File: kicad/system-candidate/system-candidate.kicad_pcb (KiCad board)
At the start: 4 copper layers, 153 x 79.1 mm, 204 parts, among them J1 691137710002 2P 5.00mm, J2 Auxiliary 12V, J3 Differential audio, J301 T1_SECONDARY, J4 Control 2x4: 3V3 RESET FAULT 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, J401 START_BUTTON, J5 691137710002 2P 5.00mm, J6 GND braid solder bond - NO mo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, K501 G6K-2F DC12, Q501 MMBT3904, Q502 MMBT3904, U1 TPA3255DDV, U2 OPA1656ID, U3 OPA1656ID, U302 LM5164DDA, U303 TPS3700DDC, U401 LP2985-33, U402 TPS3808G33, U403 TPS3808G33, U404 TPS3808G33, U405 74LVC1G14, U406 74LVC2G74, U407 74LVC2G74, U408 74LVC1G32, U409 74LVC1G07, U410 74LVC1G08, U411 74LVC1G06, U412 TPS3700DDC, U413 TPS3700DDC, U414 TPS3808G33, U415 74LVC1G08, U416 TPS3808G33, U417 74LVC2G74, U418 74LVC1G32, U419 74LVC1G07, U501 TPS3700DDC, U502 TPS3700DDC, U503 TMUX6219, U504 TPS3700DDC

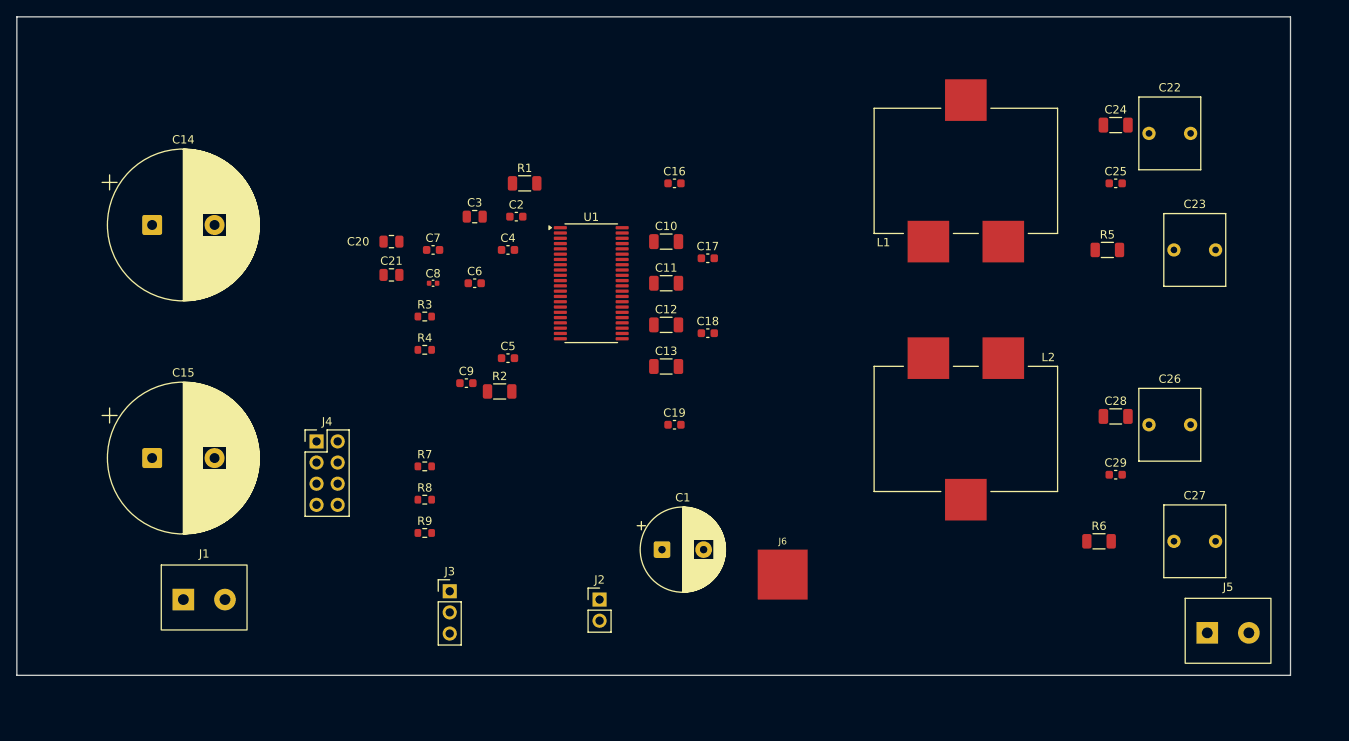
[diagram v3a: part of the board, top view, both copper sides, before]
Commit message: feat(pcb): apply measured OEM outline, M3 holes and U-profile keepout to system candidate
154x81 mm outline, 4 board-only M3 holes and F.Cu rule area OEM_U_PROFILE replace the inferred 153x79.1 study outline. DRC now shows 34 real placement conflicts (core parts inside the profile, J5 on H3): PCB-001 worklist.
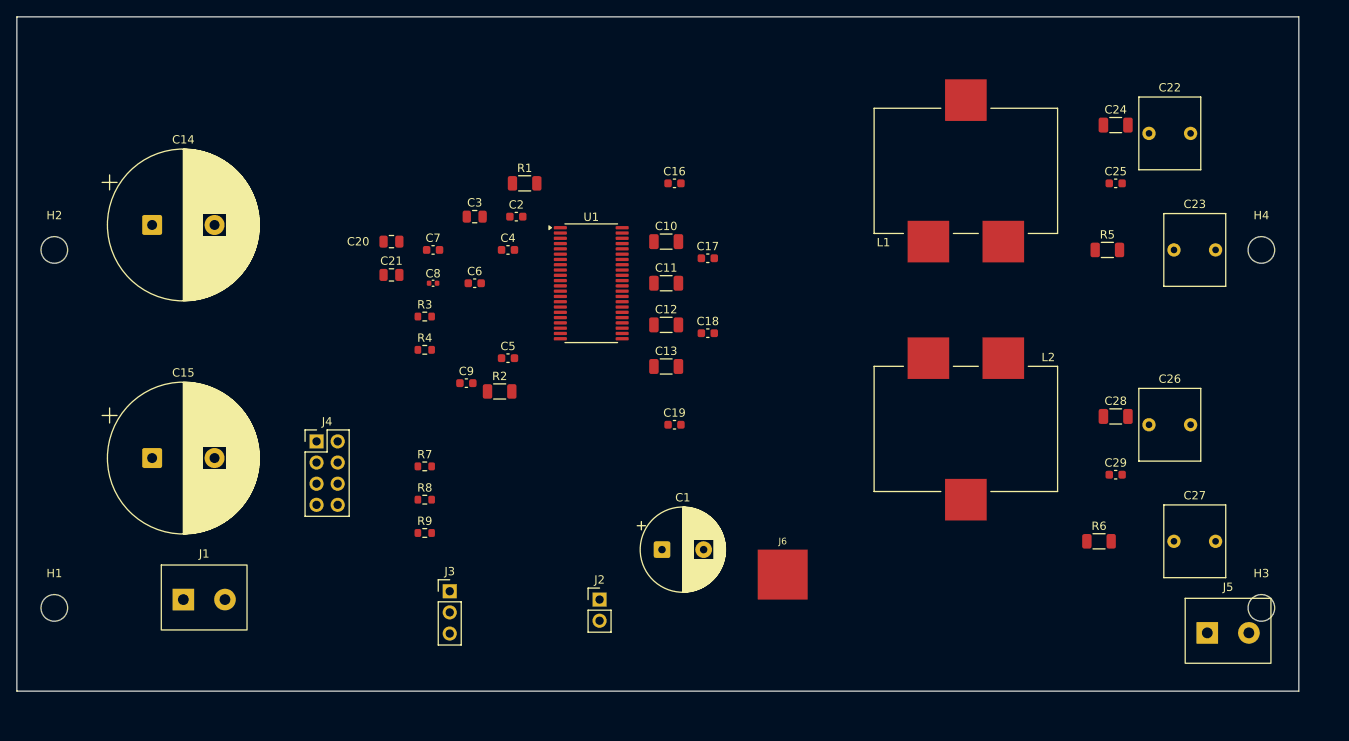
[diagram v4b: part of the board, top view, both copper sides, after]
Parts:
- added H1: OEM L-bracket M3, MountingHole:MountingHole_3.2mm_M3, F.Cu at (24.5, 91.0)
- added H2: OEM L-bracket M3, MountingHole:MountingHole_3.2mm_M3, F.Cu at (24.5, 48.0)
- added H3: OEM L-bracket M3, MountingHole:MountingHole_3.2mm_M3, F.Cu at (169.5, 91.0)
- added H4: OEM L-bracket M3, MountingHole:MountingHole_3.2mm_M3, F.Cu at (169.5, 48.0)
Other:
- board size 153 x 79.1 mm -> 154 x 81 mm
- board text added: "MEASURED OEM 154x81 (TAPE, ~1 mm) - NOT FABRICATION"
- board text added: "OEM U PROFILE 65x33 - BASE ON PCB - NO TOP PARTS"
- board text added: "TO-3P M3 (LEG FACE)"
- board text removed: "LEFT_LOWER / NO DRILL"
- board text removed: "LEFT_UPPER / NO DRILL"
- board text removed: "NO INFERRED MOUNT HOLES; J6 = SOLDERED GND BOND"
- board text removed: "OEM STUDY - 2 X CALIBRATION - NOT FABRICATION / MOUNT FIT UNVERIFIED"
- board text removed: "RIGHT FRAME STRIP: EDGE UNRESOLVED"
- board text removed: "RIGHT_LOWER / NO DRILL"
- board text removed: "RIGHT_UPPER / NO DRILL"
- board text removed: "THERMAL_LEFT / NO DRILL"
- board text removed: "THERMAL_RIGHT / NO DRILL"

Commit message: feat(pcb): study placement of all 204 parts in the measured OEM outline
Owner-confirmed orientation (x=20 relay end, x=174 transformer end). place_system_candidate.py packs power/THT on top and logic/analog SMD on the bottom; TPA3255 beside the U-profile leg. DRC: silkscreen only. README shows the latest 3D render.
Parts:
- C107, C108, C401, C402, C403, C404, C405, C406, C407, C408, C409, C410, C411, C412, C413, C414, C415, C416, C417, C418, C419, C420, C421, C422, C423, C503, C504, C505, C506, C507, C508, C509, C510, C511, C512, D501, D502, D503, D504, Q501, Q502, R101, R102, R103, R104, R105, R106, R107, R108, R202, R203, R204, R205, R206, R207, R401, R402, R403, R404, R405, R406, R407, R408, R420, R421, R422, R423, R424, R425, R426, R427, R428, R429, R430, R501, R502, R503, R504, R505, R506, R507, R508, R509, R510, R511, R512, R513, R514, R515, R516, R517, R518, U2, U3, U401, U402, U403, U404, U405, U406, U407, U408, U409, U410, U411, U412, U413, U414, U415, U416, U417, U418, U419, U501, U502, U503, U504: moved to B.Cu
- moved C410 527.6 mm to (48.4, 33.1), turned to 90 degrees
- moved U403 525.2 mm to (49.0, 37.9), turned to 90 degrees
- moved R511 518.5 mm to (85.6, 70.9)
- moved U408 517.4 mm to (56.6, 55.5)
- moved R423 509.6 mm to (70.4, 54.9), turned to 90 degrees
- moved U416 509.3 mm to (66.8, 50.9), turned to 90 degrees
- moved C421 508.2 mm to (72.1, 34.9), turned to 90 degrees
- moved R406 506.7 mm to (45.4, 34.1), turned to 90 degrees
- moved U502 506.2 mm to (89.9, 57.2)
- moved C510 503.3 mm to (94.1, 73.1)
- moved C420 502.2 mm to (52.9, 59.1)
- moved C508 501.5 mm to (89.9, 70.1)
- moved R422 500.4 mm to (57.1, 59.1)
- moved U503 497.0 mm to (90.0, 61.9)
- moved R407 496.4 mm to (77.6, 49.1), turned to 90 degrees
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
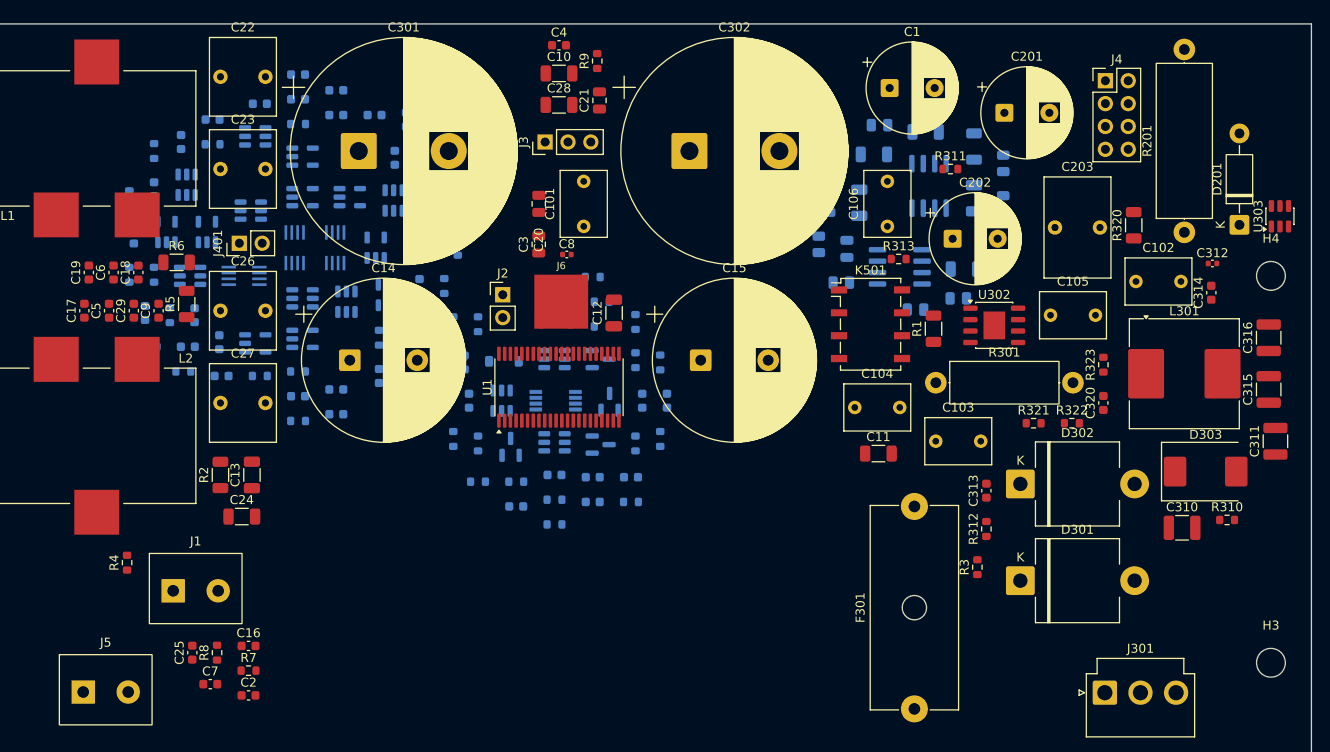
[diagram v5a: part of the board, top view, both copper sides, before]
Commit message: feat(pcb): autoroute system candidate and add datasheet envelope 3D models
make route-system: Freerouting 1.9.0 under Xvfb, 4 layers with In1 GND plane, 463/470 connections, 242 vias, DRC without clearance/short. Seven connections (TPA fine-pitch PWM/PVDD exits and four small nets) left for manual routing. Envelope VRML models for TPA3255 DDV, JST VH, WR-TBL and M3 screws from datasheet outlines; README shows the latest render.
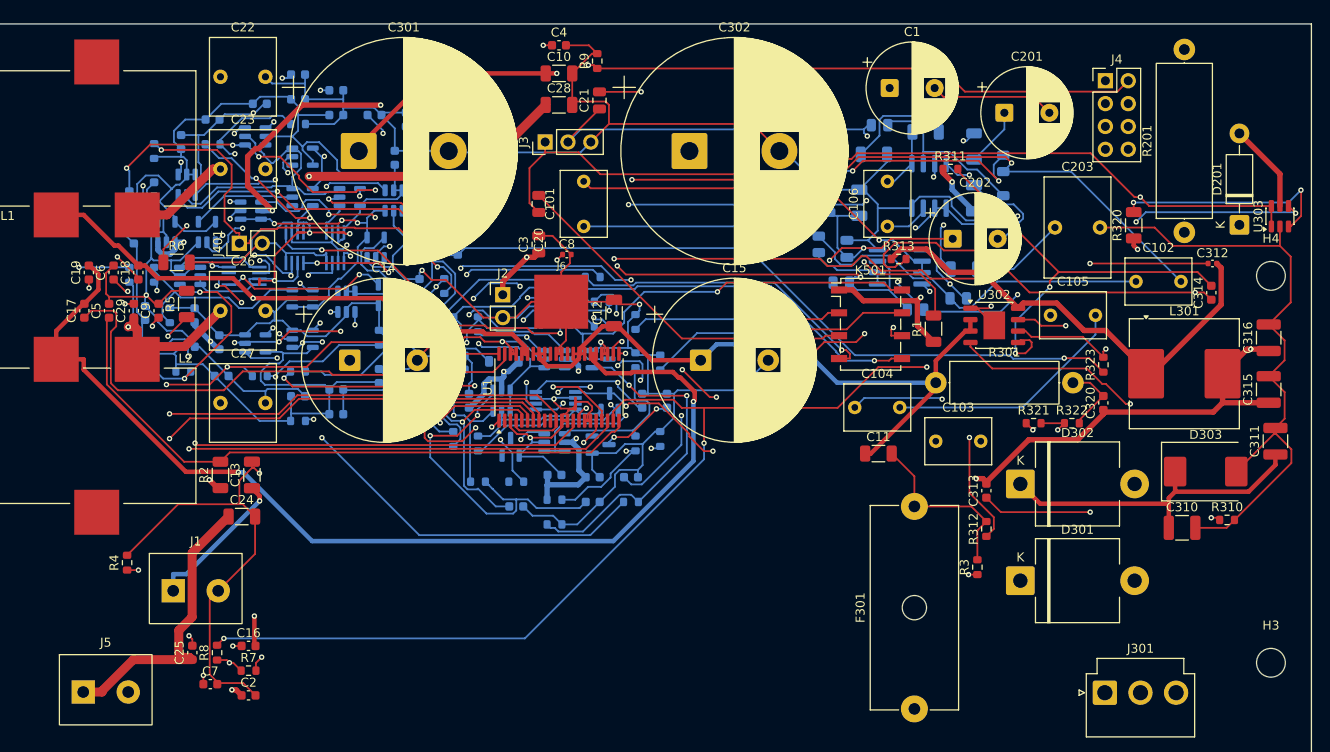
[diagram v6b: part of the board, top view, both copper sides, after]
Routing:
- net /GND: track 0.00 -> 898.9 mm, vias 0 -> 12
- net /AUX_RAW: track 0.00 -> 395.6 mm, vias 0 -> 15
- net /SEQ_3V3: track 0.00 -> 328.9 mm, vias 0 -> 4
- net /PVDD: track 0.00 -> 301.1 mm, vias 0 -> 3
- net /RAILS_OK: track 0.00 -> 236.6 mm, vias 0 -> 8
- net /FAULT: track 0.00 -> 222.9 mm, vias 0 -> 8
- net /ANALOG_12V: track 0.00 -> 213.3 mm, vias 0 -> 11
- net /VMID: track 0.00 -> 211.4 mm, vias 0 -> 10
- net /RESET: track 0.00 -> 205.2 mm, vias 0 -> 5
- net /CLIP_OTW: track 0.00 -> 199.9 mm, vias 0 -> 5
- net /VIO_3V3_EXTERNAL: track 0.00 -> 160.8 mm, vias 0 -> 1
- net /GVDD_AB: track 0.00 -> 121.5 mm, vias 0 -> 5
- net /SPK_P: track 0.00 -> 119.1 mm
- net /PWM_BD: track 0.00 -> 118.4 mm, vias 0 -> 2
- net /DIFF_P: track 0.00 -> 117.0 mm, vias 0 -> 3
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- added copper zone on In1.Cu, net /GND

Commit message: varias ataulizaçoes e correçoes
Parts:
- C301, C302: value 4700u 63V -> 4700u 63V snap-in
- D301, D302: value RECT >=400V -> MUR3040WTG
- D303: value TVS VWM>=51V -> SMCJ51A
- F301: value T8A slow -> T6.3A slow
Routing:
- net /VMID: track 211.4 -> 78.9 mm, vias 10 -> 2
- net /FAULT: track 222.9 -> 114.3 mm, vias 8 -> 6
- net /GND: track 898.9 -> 962.0 mm, vias 12 -> 9
- net /GVDD_AB: track 121.5 -> 66.8 mm, vias 5 -> 2
- net /DIVIDED: track 64.4 -> 12.3 mm, vias 5 -> 0
- net /RAILS_OK: track 236.6 -> 191.8 mm
- net /AUDIO_EN: track 41.8 -> 0.00 mm, vias 2 -> 0
- net /BST_C: track 104.2 -> 68.5 mm
- net /BST_D: track 107.9 -> 76.4 mm, vias 2 -> 4
- net /CLIP_OTW: track 199.9 -> 168.8 mm, vias 5 -> 4
- net /RESET: track 205.2 -> 177.3 mm, vias 5 -> 3
- net /OC_ADJ: track 84.5 -> 58.1 mm
- net /PWM_BD: track 118.4 -> 143.6 mm, vias 2 -> 4
- net /AUX_OV: track 17.5 -> 41.3 mm, vias 0 -> 4
- net /INA_UV: track 40.1 -> 16.7 mm, vias 4 -> 0
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
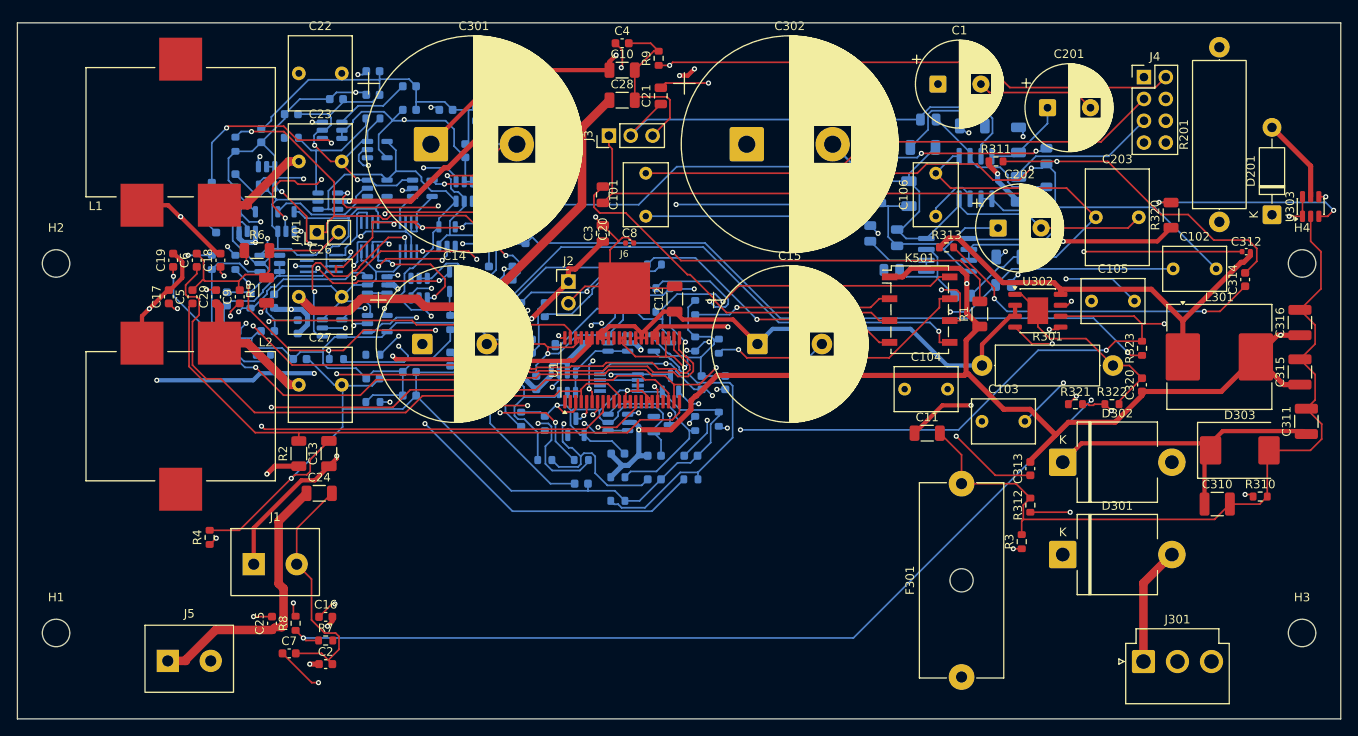
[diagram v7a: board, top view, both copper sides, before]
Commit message: feat(pcb): placa única D-030 com potência fechada e regras pragmáticas
- revoga D-029 (Rev A/Rev B) e remove kicad/rev-a-bench
- J301 JST B3P-VH (manual PS28 p.14), D301/D302 P600J, C301/C302 em footprint D30,
  F301 Littelfuse 02186.3MXP; R201 DIN0617 vertical
- ERC: pinos PBTL paralelos passive e TP101 MONO_IN (de fix/pcb-route-drc-erc)
- system-candidate regenerada: 205 footprints, ERC 0, DRC 0, paridade 0,
  471 conexões para rota manual; autoroute de estudo descartado; galeria 3D refeita
- AGENTS.md/safety/PLANNING: política de evidência pragmática e Done objetivo
- tasks SETUP-003, PCB-003, PWR-001, ELEC-001 e SYS-001 concluídas
- roteiro de medidas restantes em mechanical/measurement-request.md
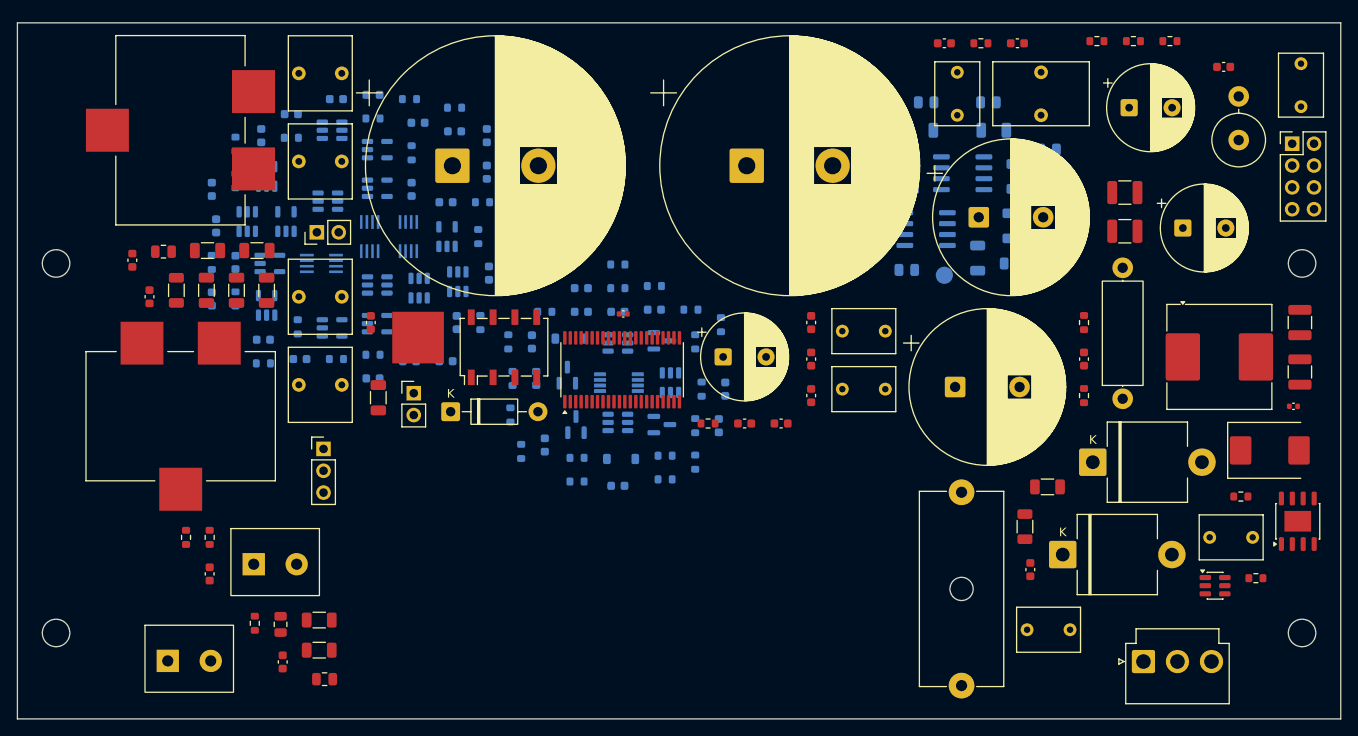
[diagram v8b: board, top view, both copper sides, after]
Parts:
- added TP101: MONO_IN, TestPoint:TestPoint_Pad_D2.0mm, B.Cu at (127.9, 49.4)
- C301, C302: footprint Capacitor_THT:CP_Radial_D25.0mm_P10.00mm_SnapIn -> Capacitor_THT:CP_Radial_D30.0mm_P10.00mm_SnapIn
- D301, D302: value MUR3040WTG -> P600J
- R201: footprint Resistor_THT:R_Axial_DIN0617_L17.0mm_D6.0mm_P20.32mm_Horizontal -> Resistor_THT:R_Axial_DIN0617_L17.0mm_D6.0mm_P5.08mm_Vertical
- moved C25 109.9 mm to (136.4, 22.4), turned to 0 degrees
- moved R7 103.2 mm to (132.1, 22.4)
- moved D201 98.3 mm to (70.4, 65.2), turned to 0 degrees
- moved R6 95.0 mm to (137.2, 78.6), turned to 90 degrees
- moved C5 92.3 mm to (127.9, 22.4), turned to 0 degrees
- moved R3 89.8 mm to (47.6, 89.9)
- moved R1 86.3 mm to (55.1, 93.0), turned to 0 degrees
- moved C11 85.5 mm to (42.0, 51.1), turned to 90 degrees
- moved C29 69.6 mm to (112.4, 59.1)
- moved C18 69.1 mm to (112.4, 54.9)
- moved C101 65.5 mm to (137.5, 90.6), turned to 0 degrees
- moved C20 65.0 mm to (55.8, 96.4), turned to 0 degrees
- moved C9 64.7 mm to (108.9, 66.6), turned to 0 degrees
- moved C14 62.2 mm to (129.1, 62.4)
- moved C16 62.1 mm to (112.4, 63.4), turned to 90 degrees
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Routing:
- net /GND: track 962.0 -> 0.00 mm, vias 9 -> 0
- net /AUX_RAW: track 412.8 -> 0.00 mm, vias 14 -> 0
- net /SEQ_3V3: track 327.3 -> 0.00 mm, vias 7 -> 0
- net /PVDD: track 307.7 -> 0.00 mm, vias 4 -> 0
- net /ANALOG_12V: track 222.9 -> 0.00 mm, vias 8 -> 0
- net /RAILS_OK: track 191.8 -> 0.00 mm, vias 8 -> 0
- net /RESET: track 177.3 -> 0.00 mm, vias 3 -> 0
- net /CLIP_OTW: track 168.8 -> 0.00 mm, vias 4 -> 0
- net /VIO_3V3_EXTERNAL: track 151.4 -> 0.00 mm, vias 2 -> 0
- net /PWM_BD: track 143.6 -> 0.00 mm, vias 4 -> 0
- net /SPK_N: track 129.2 -> 0.00 mm
- net /SPK_P: track 118.9 -> 0.00 mm
- net /PWM_AC: track 117.1 -> 0.00 mm, vias 5 -> 0
- net /RUN: track 115.4 -> 0.00 mm, vias 4 -> 0
- net /FAULT: track 114.3 -> 0.00 mm, vias 6 -> 0
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- removed copper zone on In1.Cu, net /GND
